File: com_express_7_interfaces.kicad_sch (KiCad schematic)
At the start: 8 parts, among them J1 Plug_Bus_CE7_EPT_401-51501-51

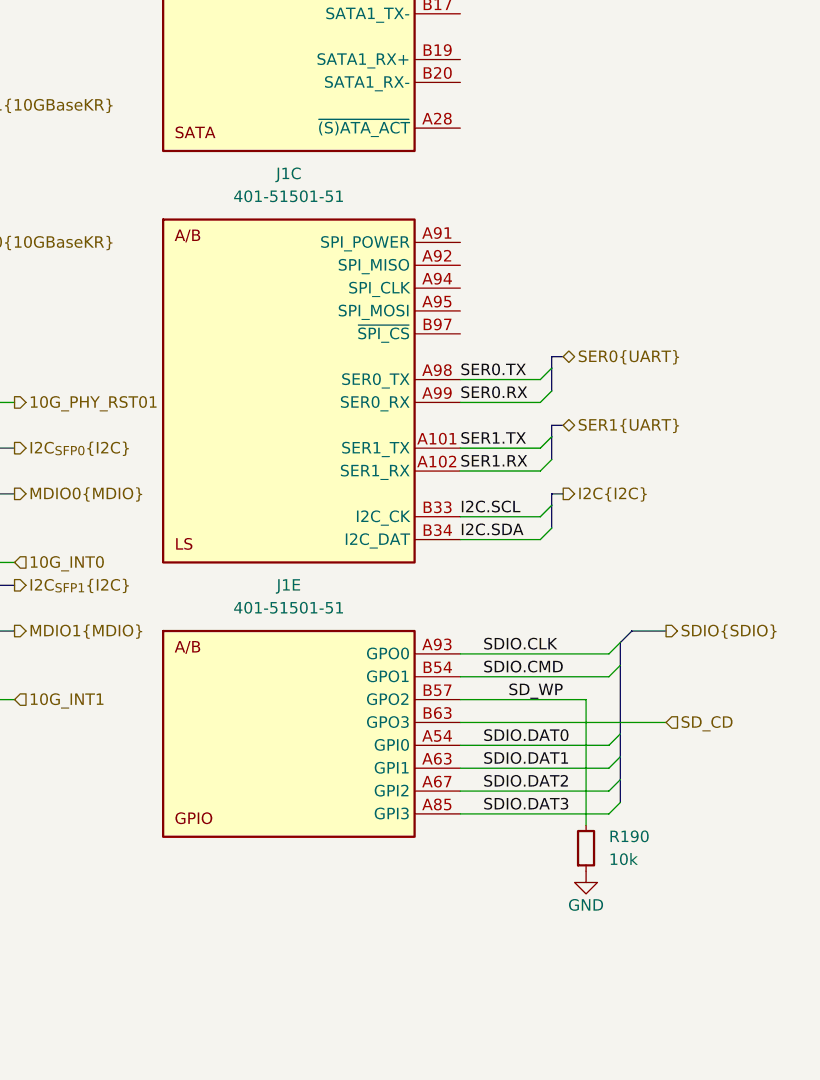
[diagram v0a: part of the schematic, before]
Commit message: [#57905] Add MAFS carrier BIOS
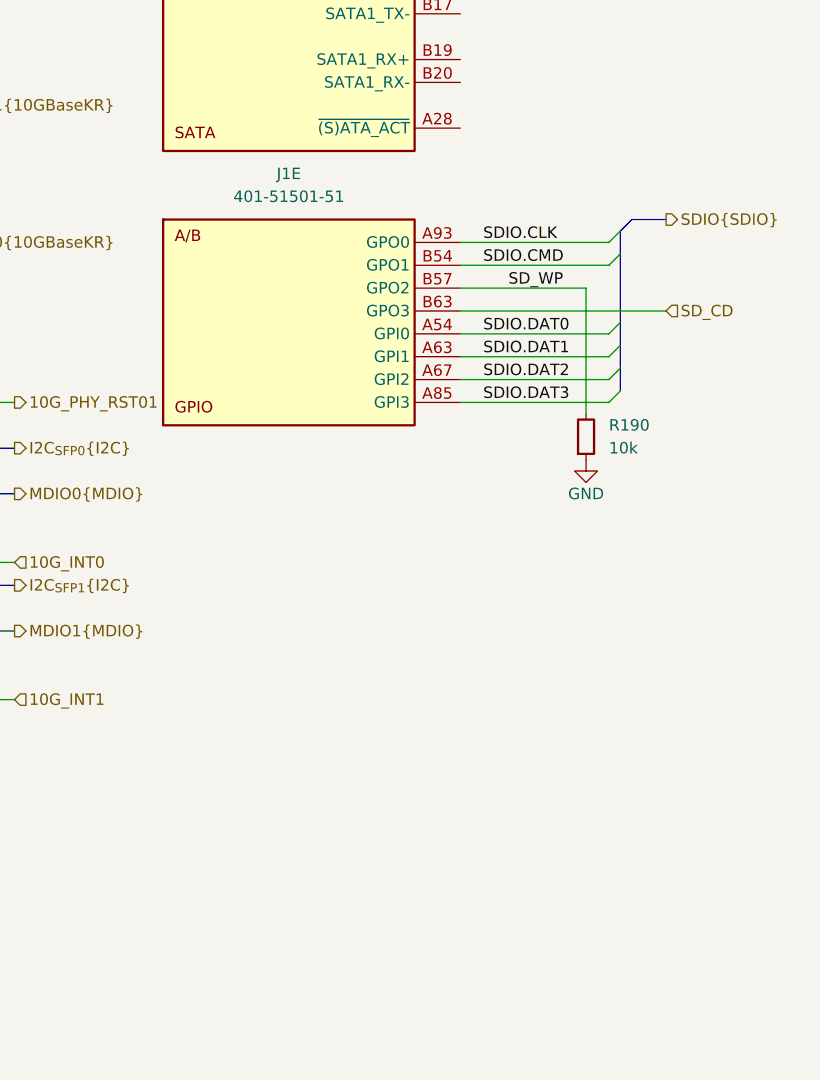
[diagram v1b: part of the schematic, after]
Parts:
- removed unit 3 of J1
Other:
- moved on the sheet: J1E, R190

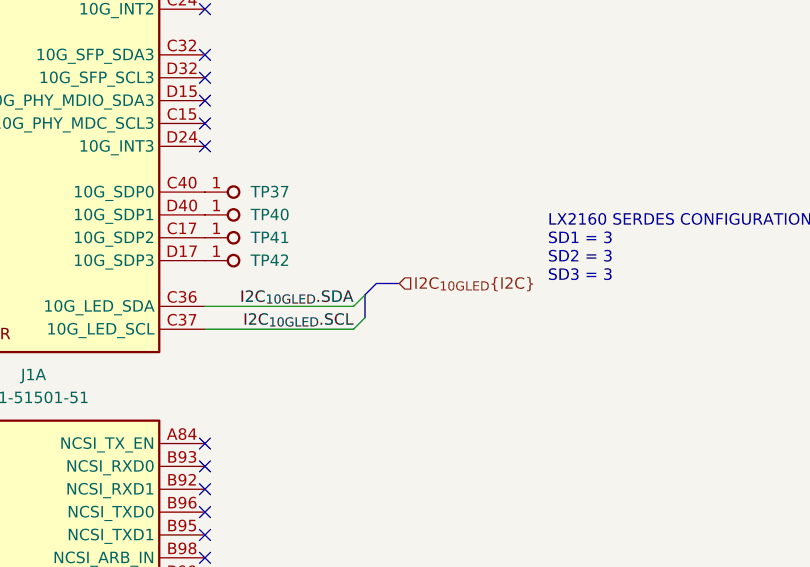
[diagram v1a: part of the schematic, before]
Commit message: [#57905] Add carrier board EEPROM
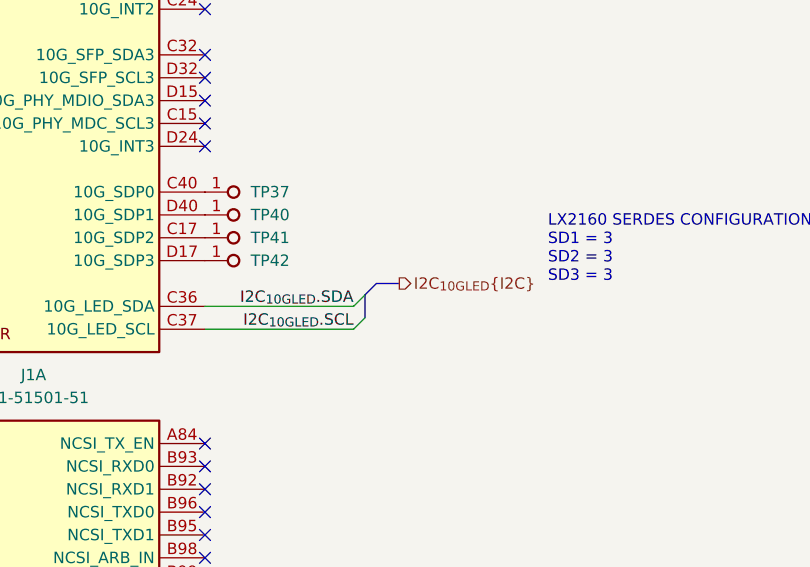
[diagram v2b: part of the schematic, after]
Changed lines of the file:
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@@
     (effects (font (size 1.27 1.27)) (justify left))
   )
-  (hierarchical_label "I2C_{10GLED}{I2C}" (shape input) (at 303.53 180.34 0) (fields_autoplaced)
+  (hierarchical_label "I2C_{10GLED}{I2C}" (shape output) (at 303.53 180.34 0) (fields_autoplaced)
     (effects (font (size 1.27 1.27)) (justify left))
   )

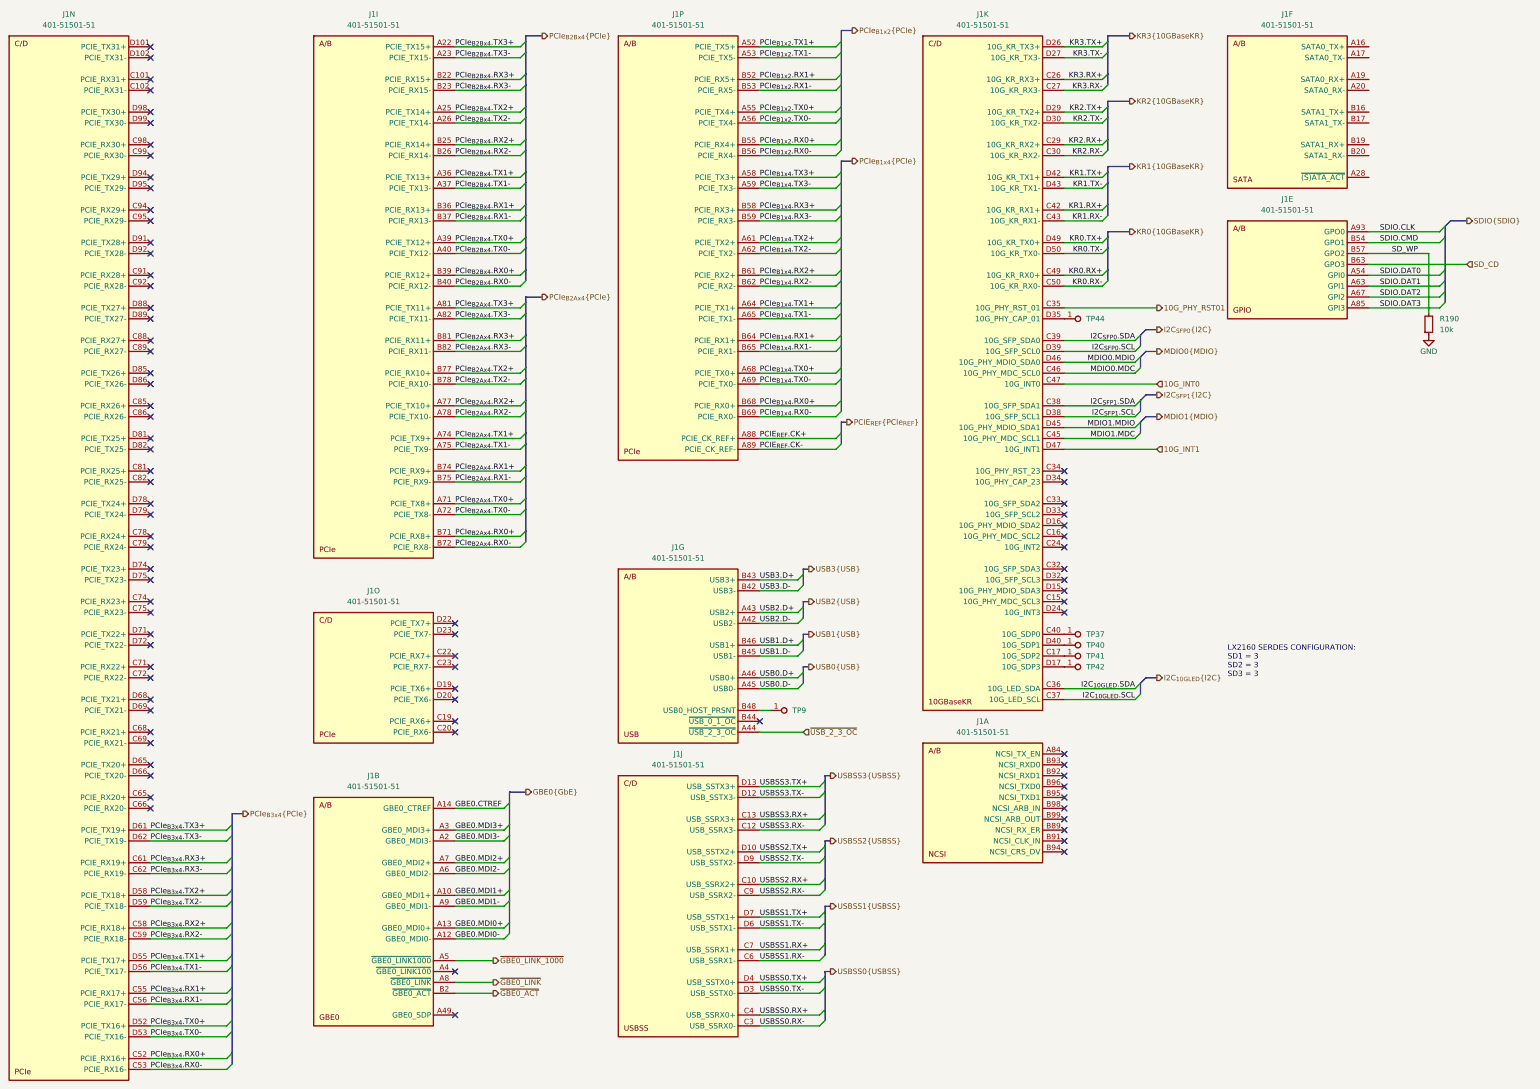
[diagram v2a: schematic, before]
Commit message: [#58137] Update backplane connector pinout
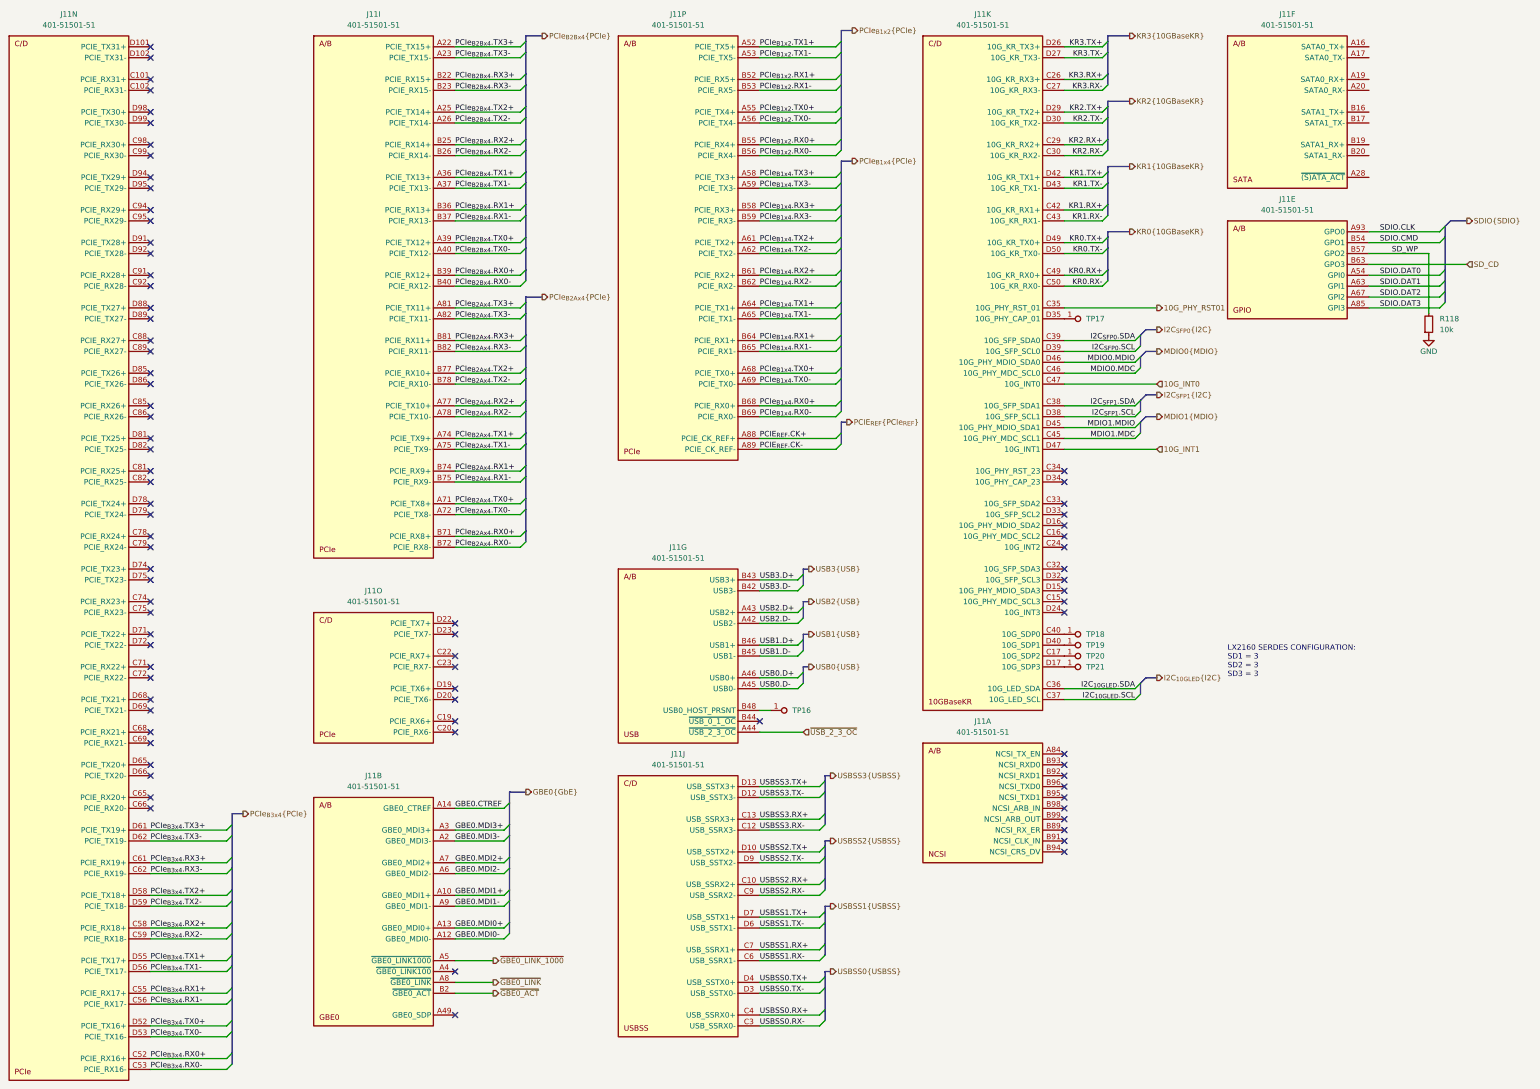
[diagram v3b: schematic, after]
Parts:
- renumbered J1 to J11, R190 to R118, TP9 to TP16, TP44 to TP17, TP37 to TP18, TP40 to TP19, TP41 to TP20, TP42 to TP21

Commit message: Fix ERC
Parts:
- J11: Manufacturer EPT -> ept
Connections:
- net PCIe_{B2Ax4}.RX2+: now also J11.B77 (PCIE_RX10+); no longer J11.A77 (PCIE_TX10+)
- net PCIe_{B2Ax4}.RX2-: now also J11.B78 (PCIE_RX10-); no longer J11.A78 (PCIE_TX10-)
- net PCIe_{B2Ax4}.TX2+: now also J11.A77 (PCIE_TX10+); no longer J11.B77 (PCIE_RX10+)
- net PCIe_{B2Ax4}.TX2-: now also J11.A78 (PCIE_TX10-); no longer J11.B78 (PCIE_RX10-)
- net KR2.RX+: no longer names the net of J11.C29 (10G_KR_RX2+)
- net KR2.RX-: no longer names the net of J11.C30 (10G_KR_RX2-)
- net KR2.TX+: no longer names the net of J11.D29 (10G_KR_TX2+)
- net KR2.TX-: no longer names the net of J11.D30 (10G_KR_TX2-)
- net KR3.RX+: no longer names the net of J11.C26 (10G_KR_RX3+)
- net KR3.RX-: no longer names the net of J11.C27 (10G_KR_RX3-)
- net KR3.TX+: no longer names the net of J11.D26 (10G_KR_TX3+)
- net KR3.TX-: no longer names the net of J11.D27 (10G_KR_TX3-)
- net USBSS0.RX+: no longer names the net of J11.C4 (USB_SSRX0+)
- net USBSS0.RX-: no longer names the net of J11.C3 (USB_SSRX0-)
- net USBSS0.TX+: no longer names the net of J11.D4 (USB_SSTX0+)
- net USBSS0.TX-: no longer names the net of J11.D3 (USB_SSTX0-)
- net USBSS1.RX+: no longer names the net of J11.C7 (USB_SSRX1+)
- net USBSS1.RX-: no longer names the net of J11.C6 (USB_SSRX1-)
- net USBSS1.TX+: no longer names the net of J11.D7 (USB_SSTX1+)
- net USBSS1.TX-: no longer names the net of J11.D6 (USB_SSTX1-)
- no-connect marks 81 -> 106
